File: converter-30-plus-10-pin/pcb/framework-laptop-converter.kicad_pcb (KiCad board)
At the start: 4 copper layers, 19.1 x 36 mm, 7 parts, among them J1 20879-040E-01, J2 FFC2B28-40-G

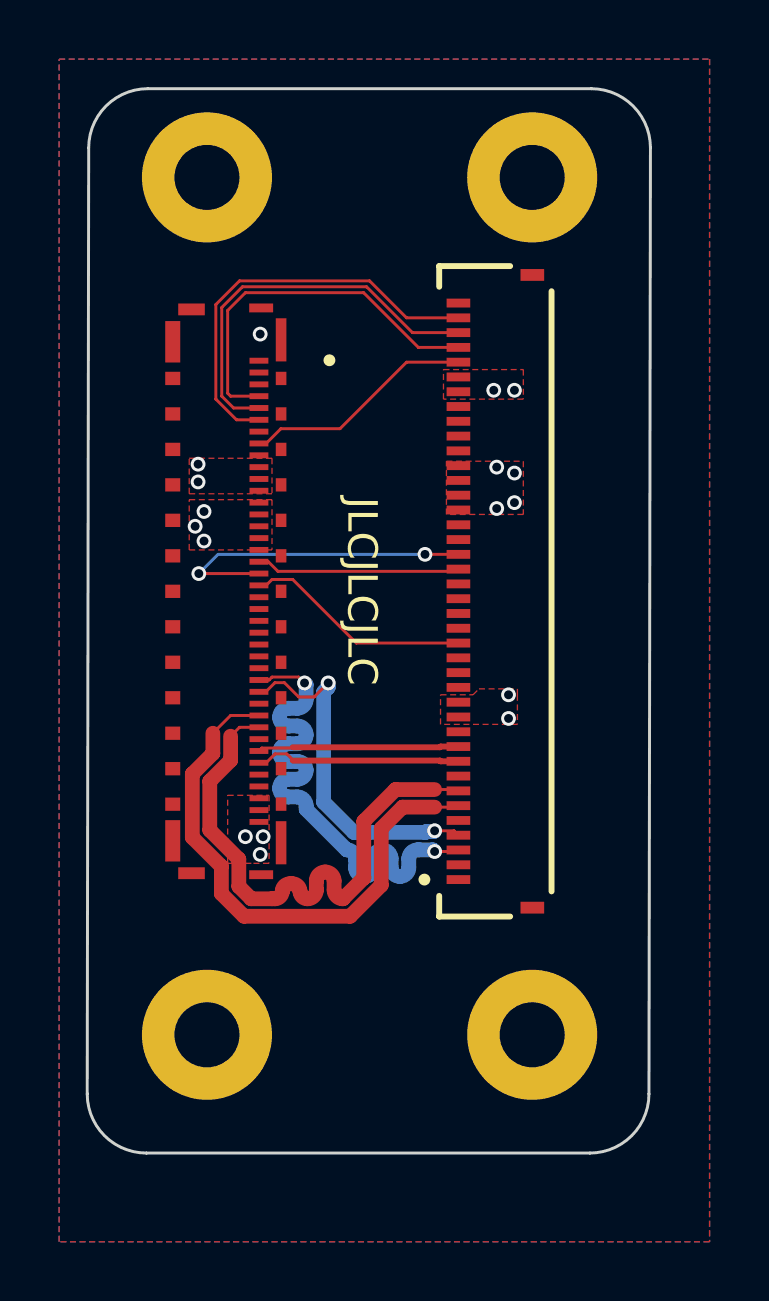
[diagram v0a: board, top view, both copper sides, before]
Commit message: converter was crooked
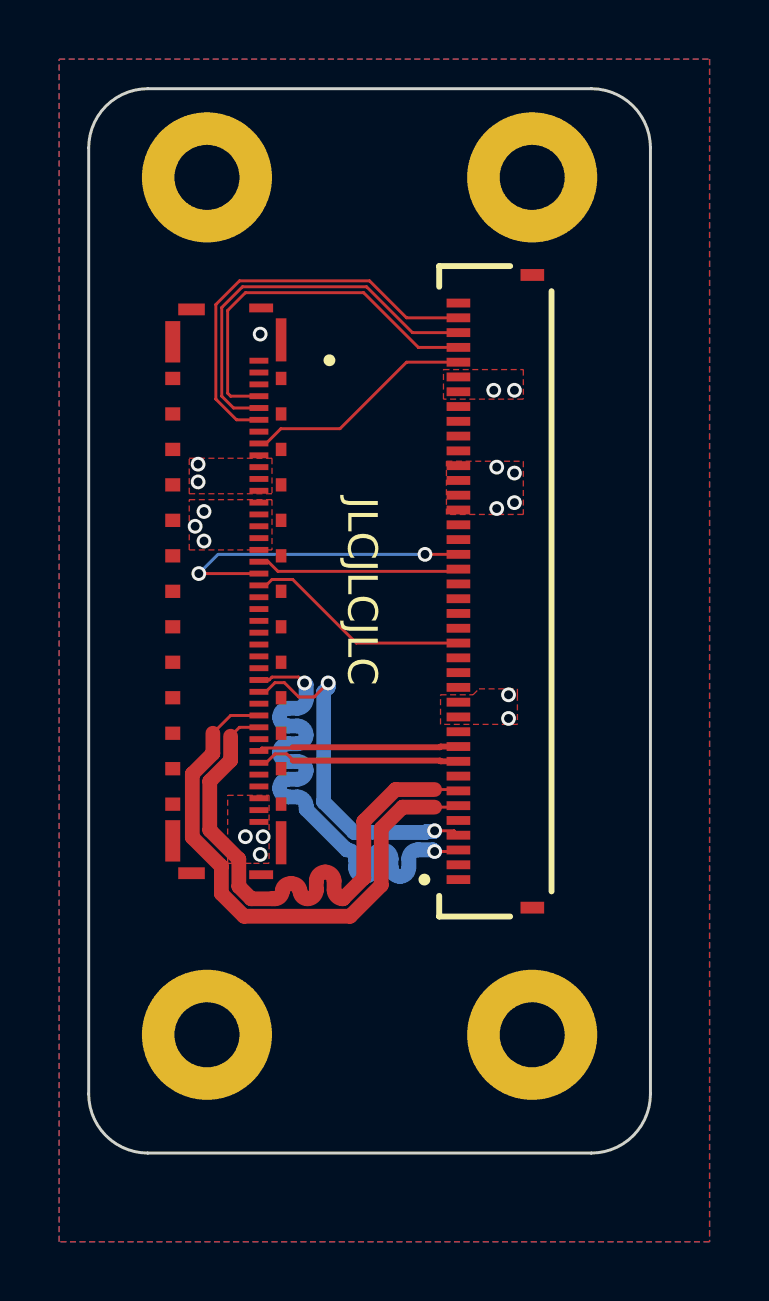
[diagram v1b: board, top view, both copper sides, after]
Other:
- board size 19.1 x 36 mm -> 19 x 36 mm
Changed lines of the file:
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@@
   )
   (gr_arc (start 150 82) (mid 151.414214 82.585786) (end 152 84) (layer "Edge.Cuts") (width 0.1))
-  (gr_arc (start 151.95 116) (mid 151.364214 117.414214) (end 149.95 118) (layer "Edge.Cuts") (width 0.1))
-  (gr_line (start 132.95 116) (end 133 84) (layer "Edge.Cuts") (width 0.1))
-  (gr_line (start 149.95 118) (end 134.95 118) (layer "Edge.Cuts") (width 0.1))
-  (gr_arc (start 134.95 118) (mid 133.535786 117.414214) (end 132.95 116) (layer "Edge.Cuts") (width 0.1))
-  (gr_line (start 151.95 116) (end 152 84) (layer "Edge.Cuts") (width 0.1))
+  (gr_arc (start 152 116) (mid 151.414214 117.414214) (end 150 118) (layer "Edge.Cuts") (width 0.1))
+  (gr_line (start 133 116) (end 133 84) (layer "Edge.Cuts") (width 0.1))
+  (gr_line (start 150 118) (end 135 118) (layer "Edge.Cuts") (width 0.1))
+  (gr_arc (start 135 118) (mid 133.585786 117.414214) (end 133 116) (layer "Edge.Cuts") (width 0.1))
+  (gr_line (start 152 116) (end 152 84) (layer "Edge.Cuts") (width 0.1))
   (gr_line (start 150 82) (end 135 82) (layer "Edge.Cuts") (width 0.1))
   (gr_arc (start 133 84) (mid 133.585786 82.585786) (end 135 82) (layer "Edge.Cuts") (width 0.1))
